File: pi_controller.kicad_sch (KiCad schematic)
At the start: 159 parts, among them J1 PWM, J2 DC Supply, J26 LED6, J27 LED5, J28 LED7, J29 LED8, J30 I2C, J31 UART, J32 LED3, J33 LED1, J34 LED2, J35 LED4, Q1 AOD4184A, Q2 MMBT3904, U1 AP62300TWU, U2 CD74HC4067SM96, U3 LM4040DBZ-3, U4 RaspberryPi_Pico, U5 74HC138, U6 TM1639 (TA2009B), U7 74HC138

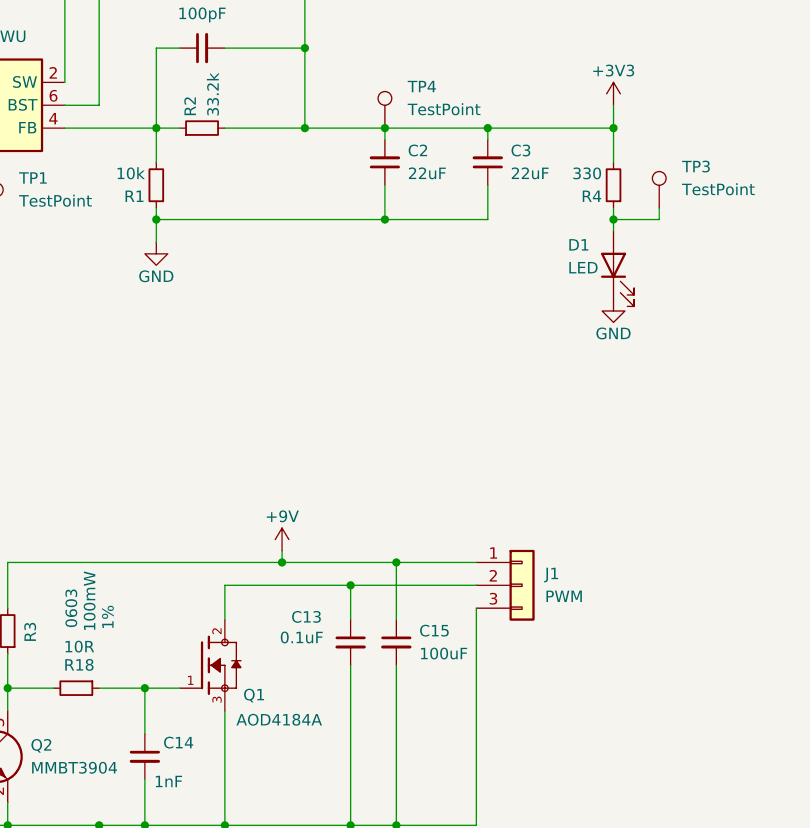
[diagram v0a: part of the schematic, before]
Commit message: Adjusting footprints for production
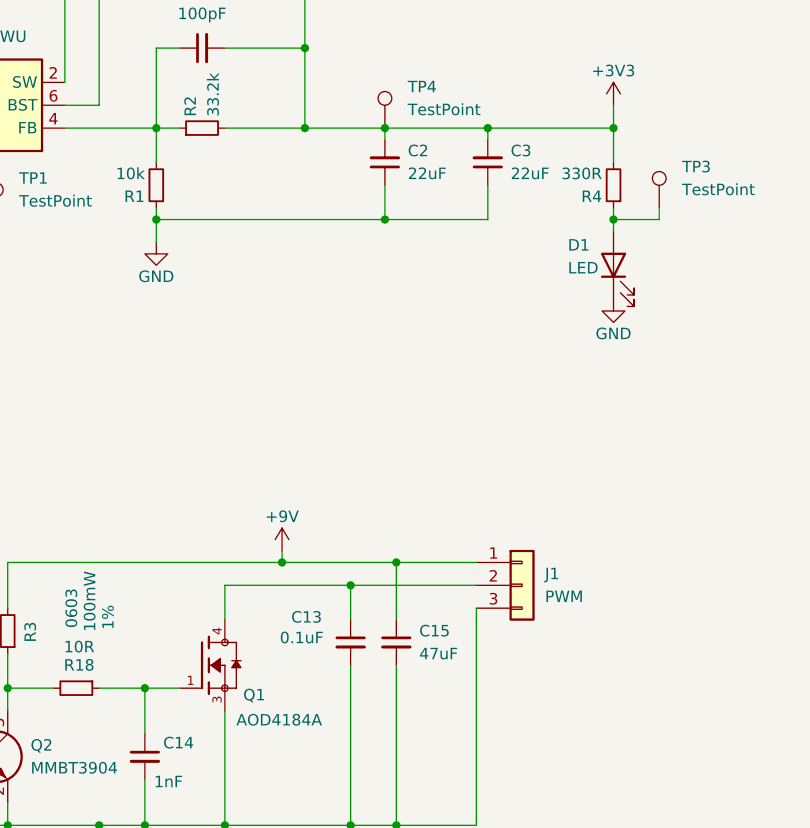
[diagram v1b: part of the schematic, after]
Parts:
- AN1, AN10, AN11, AN12, AN13, AN14, AN15, AN16, AN2, AN3, AN4, AN5, AN6, AN7, AN8, AN9: JLCPCB Part # C495558 -> (none); LCSC PN (none) -> C495558
- C1, C11, C12, C13: footprint Capacitor_SMD:C_0201_0603Metric_Pad0.64x0.40mm_HandSolder -> Capacitor_SMD:C_0603_1608Metric_Pad1.08x0.95mm_HandSolder; JLCPCB Part # C14663 -> (none); LCSC PN (none) -> C14663
- C10: footprint Capacitor_SMD:C_0201_0603Metric_Pad0.64x0.40mm_HandSolder -> Capacitor_SMD:C_1206_3216Metric_Pad1.33x1.80mm_HandSolder; JLCPCB Part # C14663 -> (none); LCSC PN (none) -> C15008; Package 0603 -> 1206
- C14: footprint Capacitor_SMD:C_0201_0603Metric_Pad0.64x0.40mm_HandSolder -> Capacitor_SMD:C_0603_1608Metric_Pad1.08x0.95mm_HandSolder; JLCPCB Part # C1588 -> (none); LCSC PN (none) -> C1588
- C15: value 100uF -> 47uF; footprint Capacitor_SMD:C_0201_0603Metric_Pad0.64x0.40mm_HandSolder -> Capacitor_SMD:C_1206_3216Metric_Pad1.33x1.80mm_HandSolder; JLCPCB Part # C14663 -> (none); LCSC PN (none) -> C76659; Package 0603 -> 1206
- C2, C3: JLCPCB Part # C12891 -> (none); LCSC PN (none) -> C12891
- C4: JLCPCB Part # C13585 -> (none); LCSC PN (none) -> C13585
- C5: JLCPCB Part # C1623 -> (none); LCSC PN (none) -> C1623
- C6: JLCPCB Part # C21120 -> (none); LCSC PN (none) -> C21120
- C7: footprint Capacitor_SMD:C_0201_0603Metric_Pad0.64x0.40mm_HandSolder -> Capacitor_SMD:C_0603_1608Metric_Pad1.08x0.95mm_HandSolder; JLCPCB Part # C14663 -> (none); LCSC PN (none) -> C14858
- C8: footprint Capacitor_SMD:C_0201_0603Metric_Pad0.64x0.40mm_HandSolder -> Capacitor_SMD:C_0603_1608Metric_Pad1.08x0.95mm_HandSolder; JLCPCB Part # C23630 -> (none); LCSC PN (none) -> C23630
- C9: footprint Capacitor_SMD:C_0201_0603Metric_Pad0.64x0.40mm_HandSolder -> Capacitor_SMD:C_0603_1608Metric_Pad1.08x0.95mm_HandSolder; JLCPCB Part # C14663 -> (none); LCSC PN (none) -> C14663; Tolerance 10% -> 5%
- D1: JLCPCB Part # C2297 -> (none); LCSC PN (none) -> C2297
- D10, D11, D12, D13, D14, D15, D16, D17, D18, D19, D2, D20, D21, D22, D23, D24, D25, D26, D27, D28, D29, D3, D30, D31, D32, D33, D34, D35, D36, D37, D38, D39, D4, D40, D41, D42, D43, D44, D45, D46, D47, D48, D49, D5, D50, D51, D52, D53, D54, D55, D56, D57, D58, D59, D6, D60, D61, D62, D63, D64, D65, D7, D8, D9: JLCPCB Part # C358488 -> (none); LCSC PN (none) -> C358488
- J1: JLCPCB Part # C49257 -> (none); LCSC PN (none) -> C49257
- J2: JLCPCB Part # C381116 -> (none); LCSC PN (none) -> C381116
- J26, J27, J28, J29, J32, J33, J34, J35, JR1, JR2, JR3, JR4, JR5, JR6, JR7, JR8: LCSC PN (none) -> C779499
- J30, J31: JLCPCB Part # C163034 -> (none); LCSC PN (none) -> C163034
- JSPI1, JSPI2, JSPI3, JSPI4, JSPI5, JSPI6, JSPI7: JLCPCB Part # C495631 -> (none); LCSC PN (none) -> C495631
- L1: JLCPCB Part # C5189747 -> (none); LCSC PN (none) -> C5189747
- Q1: footprint Package_TO_SOT_SMD:TO-252-2 -> AOD4184A:DPAK228P994X240-4N; JLCPCB Part # C99124 -> (none); LCSC PN (none) -> C99124
- Q2: LCSC PN (none) -> C20526
- R1, R5: JLCPCB Part # C25804 -> (none); LCSC PN (none) -> C25804
- R10, R11, R12, R13, R14, R15, R16, R9: JLCPCB Part # C22978 -> (none); LCSC PN (none) -> C22978
- R17, R7, R8: JLCPCB Part # C4190 -> (none); LCSC PN (none) -> C4190
- R18: JLCPCB Part # C873673 -> (none); LCSC PN (none) -> C22859
- R2: JLCPCB Part # C23003 -> (none); LCSC PN (none) -> C23003
- R3: JLCPCB Part # C543357 -> (none); LCSC PN (none) -> C543357
- R4: value 330 -> 330R; JLCPCB Part # C23137 -> (none); LCSC PN (none) -> C23138
- R6: JLCPCB Part # C23182 -> (none); LCSC PN (none) -> C23182
- U1: JLCPCB Part # C1883519 -> (none); LCSC PN (none) -> C1883519
- U2: JLCPCB Part # C98457 -> (none); LCSC PN (none) -> C98457
- U3: JLCPCB Part # C460608 -> (none); LCSC PN (none) -> C460608
- U4: footprint Module_RaspberryPi_Pico:RaspberryPi_Pico_Common_THT -> PiMatrix:RaspberryPi_Pico_Common_THT_CustomSilk; now left out of the parts list
- U5, U7: JLCPCB Part # C6818 -> (none); LCSC PN (none) -> C6818
- U6: JLCPCB Part # C20611984 -> (none); LCSC PN (none) -> C20611984
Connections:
- net at C13.1, J1.2 (Pin_2): now also Q1.4; no longer Q1.2

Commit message: Project name change to signalbridge and board final revision
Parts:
- AN1, AN10, AN11, AN12, AN13, AN14, AN15, AN16, AN2, AN3, AN4, AN5, AN6, AN7, AN8, AN9: footprint PiMatrix:JST_ZH_B3B-ZR_1x03_P1.50mm_Vertical_SilkSafe -> pi_controller:JST_ZH_B3B-ZR_1x03_P1.50mm_Vertical_SilkSafe
- J2: footprint Connector_BarrelJack:BarrelJack_Horizontal -> pi_controller:BarrelJack_Horizontal
- J26, J27, J28, J29, J32, J33, J34, J35, JR1, JR2, JR3, JR4, JR5, JR6, JR7, JR8: footprint Connector_PinHeader_2.54mm:PinHeader_2x08_P2.54mm_Vertical -> pi_controller:PinHeader_2x08_P2.54mm_Vertical
- J30, J31: footprint PiMatrix:JST_ZH_B4B-ZR_1x04_P1.50mm_Vertical_SilkSafe -> pi_controller:JST_ZH_B4B-ZR_1x04_P1.50mm_Vertical_SilkSafe
- JSPI1, JSPI2, JSPI3, JSPI4, JSPI5, JSPI6, JSPI7: footprint PiMatrix:JST_ZH_B6B-ZR_1x06_P1.50mm_Vertical_SilkSafe -> pi_controller:JST_ZH_B6B-ZR_1x06_P1.50mm_Vertical_SilkSafe
- U4: footprint PiMatrix:RaspberryPi_Pico_Common_THT_CustomSilk -> pi_controller:RaspberryPi_Pico_Common_THT_CustomSilk

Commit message: Changed part number (out of stock)
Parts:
- J26, J27, J28, J29, J32, J33, J34, J35, JR1, JR2, JR3, JR4, JR5, JR6, JR7, JR8: LCSC PN C779499 -> C68234
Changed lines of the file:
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@@
 			)
 		)
-		(property "LCSC PN" "C779499"
+		(property "LCSC PN" "C68234"
 			(at 472.44 236.22 0)
 			(effects
@@
 			)
 		)
-		(property "LCSC PN" "C779499"
+		(property "LCSC PN" "C68234"
 			(at 367.03 149.86 0)
 			(effects
@@
 			)
 		)
-		(property "LCSC PN" "C779499"
+		(property "LCSC PN" "C68234"
 			(at 400.05 121.92 0)
 			(effects
@@
 			)
 		)
-		(property "LCSC PN" "C779499"
+		(property "LCSC PN" "C68234"
 			(at 383.54 276.86 0)
 			(effects
@@
 			)
 		)
-		(property "LCSC PN" "C779499"
+		(property "LCSC PN" "C68234"
 			(at 400.05 180.34 0)
 			(effects
@@
 			)
 		)
-		(property "LCSC PN" "C779499"
+		(property "LCSC PN" "C68234"
 			(at 295.91 320.04 0)
 			(effects
@@
 			)
 		)
-		(property "LCSC PN" "C779499"
+		(property "LCSC PN" "C68234"
 			(at 472.44 278.13 0)
 			(effects
@@
 			)
 		)
-		(property "LCSC PN" "C779499"
+		(property "LCSC PN" "C68234"
 			(at 367.03 179.07 0)
 			(effects
@@
 			)
 		)
-		(property "LCSC PN" "C779499"
+		(property "LCSC PN" "C68234"
 			(at 295.91 276.86 0)
 			(effects
@@
 			)
 		)
-		(property "LCSC PN" "C779499"
+		(property "LCSC PN" "C68234"
 			(at 295.91 234.95 0)
 			(effects
@@
 			)
 		)
-		(property "LCSC PN" "C779499"
+		(property "LCSC PN" "C68234"
 			(at 367.03 91.44 0)
 			(effects
@@
 			)
 		)
-		(property "LCSC PN" "C779499"
+		(property "LCSC PN" "C68234"
 			(at 367.03 120.65 0)
 			(effects
@@
 			)
 		)
-		(property "LCSC PN" "C779499"
+		(property "LCSC PN" "C68234"
 			(at 383.54 320.04 0)
 			(effects
@@
 			)
 		)
-		(property "LCSC PN" "C779499"
+		(property "LCSC PN" "C68234"
 			(at 400.05 151.13 0)
 			(effects
@@
 			)
 		)
-		(property "LCSC PN" "C779499"
+		(property "LCSC PN" "C68234"
 			(at 400.05 92.71 0)
 			(effects
@@
 			)
 		)
-		(property "LCSC PN" "C779499"
+		(property "LCSC PN" "C68234"
 			(at 383.54 234.95 0)
 			(effects

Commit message: Created the slot for the pi and udpated silk screen
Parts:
- added J3, J4: Conn_01x20, Connector_PinHeader_2.54mm:PinHeader_1x20_P2.54mm_Vertical, symbol Connector_Generic:Conn_01x20
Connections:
- net ADC0: now also J4.11 (Pin_11)
- net ADC_MUX_A: now also J4.6 (Pin_6)
- net ADC_MUX_B: now also J4.7 (Pin_7)
- net ADC_MUX_C: now also J4.9 (Pin_9)
- net ADC_MUX_D: now also J3.15 (Pin_15)
- net COL_MUX_A: now also J3.11 (Pin_11)
- net COL_MUX_B: now also J3.12 (Pin_12)
- net COL_MUX_C: now also J3.14 (Pin_14)
- net CS_KEY: now also J4.2 (Pin_2)
- net CS_LED: now also J4.12 (Pin_12)
- net GND: now also J3.13 (Pin_13), J4.13 (Pin_13)
- net MISO: now also J4.1 (Pin_1)
- net MOSI: now also J4.5 (Pin_5)
- net PWM_OUT: now also J4.14 (Pin_14)
- net ROW1: now also J3.1 (Pin_1)
- net ROW2: now also J3.2 (Pin_2)
- net ROW3: now also J3.4 (Pin_4)
- net ROW4: now also J3.5 (Pin_5)
- net ROW5: now also J3.9 (Pin_9)
- net ROW6: now also J3.10 (Pin_10)
- net ROW7: now also J3.19 (Pin_19)
- net ROW8: now also J3.20 (Pin_20)
- net SCL: now also J3.7 (Pin_7)
- net SCLK: now also J4.4 (Pin_4)
- net SDA: now also J3.6 (Pin_6)
- net UART0_RX: now also J3.17 (Pin_17)
- net UART0_TX: now also J3.16 (Pin_16)
- net VDDA: now also J4.15 (Pin_15)
- no-connect marks 8 -> 19

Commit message: Adjusting testpoint pads and adding 74hc4051 datasheet
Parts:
- added C16: 0.1uF, Capacitor_SMD:C_0603_1608Metric_Pad1.08x0.95mm_HandSolder, symbol Device:C_Small
- added U8: CD74HC4051M96, Package_SO:SOIC-16_3.9x9.9mm_P1.27mm, symbol 74xx:74HC4051
- J3, J4: LCSC PN (none) -> C5224030
- TP1, TP2, TP3, TP4: footprint TestPoint:TestPoint_Pad_D4.0mm -> pi_controller:TestPoint_Pad_D2.0mm
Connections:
- net +3V3: now also C16.1, U8.16 (VCC)
- net COL_MUX_A: now also J3.1 (Pin_1), U4.1 (GPIO0); no longer J3.11 (Pin_11), U4.11 (GPIO8), U5.1 (A0)
- net COL_MUX_B: now also J3.2 (Pin_2), U4.2 (GPIO1); no longer J3.12 (Pin_12), U4.12 (GPIO9), U5.2 (A1)
- net COL_MUX_C: now also J3.4 (Pin_4), U4.4 (GPIO2); no longer J3.14 (Pin_14), U4.14 (GPIO10), U5.3 (A2)
- net GND: now also C16.2, U8.7 (VEE), U8.8 (GND)
- net ROW1: now also U8.13 (A0); no longer J3.1 (Pin_1), U4.1 (GPIO0)
- net ROW2: now also U8.14 (A1); no longer J3.2 (Pin_2), U4.2 (GPIO1)
- net ROW3: now also U8.15 (A2); no longer J3.4 (Pin_4), U4.4 (GPIO2)
- net ROW4: now also U8.12 (A3); no longer J3.5 (Pin_5), U4.5 (GPIO3)
- net ROW5: now also U8.1 (A4); no longer J3.9 (Pin_9), U4.9 (GPIO6)
- net ROW6: now also U8.5 (A5); no longer J3.10 (Pin_10), U4.10 (GPIO7)
- net ROW7: now also U8.2 (A6); no longer J3.19 (Pin_19), U4.19 (GPIO14)
- net ROW8: now also U8.4 (A7); no longer J3.20 (Pin_20), U4.20 (GPIO15)
- net CS_KEY renamed CS_COL
- net CS_LED renamed SPI_MUX_CS
- new net CS_ROW: J3.11 (Pin_11), U4.11 (GPIO8), U8.6 (~{E})
- new net ROW_INPUT: J3.12 (Pin_12), U4.12 (GPIO9), U8.3 (A)
- new net ROW_MUX_A: J3.9 (Pin_9), U4.9 (GPIO6), U8.11 (S0)
- new net ROW_MUX_B: J3.10 (Pin_10), U4.10 (GPIO7), U8.10 (S1)
- new net ROW_MUX_C: J3.5 (Pin_5), U4.5 (GPIO3), U8.9 (S2)
- new net SPI_MUX_A: J3.14 (Pin_14), U4.14 (GPIO10), U5.1 (A0)
- new net SPI_MUX_B: J3.19 (Pin_19), U4.19 (GPIO14), U5.2 (A1)
- new net SPI_MUX_C: J3.20 (Pin_20), U4.20 (GPIO15), U5.3 (A2)
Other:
- moved on the sheet: C12, U7

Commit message: Upgrading power supply protection
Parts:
- added C17: 22uF, Capacitor_SMD:C_1206_3216Metric_Pad1.33x1.80mm_HandSolder, symbol Device:C_Small
- added D66: Z2SMBJ18A, Diode_SMD:D_SMB, symbol Diode:Z2SMBxxx
- added D67: BZT52C12, Diode_SMD:D_SOD-123, symbol Diode:BZT52Bxx
- added F1: Polyfuse, Fuse:Fuse_1210_3225Metric_Pad1.42x2.65mm_HandSolder, symbol Device:Polyfuse
- added JP1: Jumper_2_Open, Jumper:SolderJumper-2_P1.3mm_Open_TrianglePad1.0x1.5mm, symbol Jumper:Jumper_2_Open
- added Q3: AO4407A, AO4407A:SOIC127P600X175-8N, symbol AO4407A:AO4407A
- added R19, R20, R21, R22, R23, R24, R25, R26, R27, R28, R29: 4.7k, Resistor_SMD:R_0603_1608Metric_Pad0.98x0.95mm_HandSolder, symbol Device:R_Small
- added R30: 10k, Resistor_SMD:R_0603_1608Metric_Pad0.98x0.95mm_HandSolder, symbol Device:R_Small
- added TP5, TP6: TestPoint, pi_controller:TestPoint_Pad_D2.0mm, symbol Connector:TestPoint
- C15: Voltage Rating 50V -> 25V
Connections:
- net +3V3: now also R19.1, R20.1, R21.1, R22.1, R23.1, R24.1, R25.1, R26.1, R27.1, R28.1, R29.1
- net +9V: now also F1.1; no longer C4.2, U1.3 (IN)
- net CS1: now also R19.2
- net CS2: now also R20.2
- net CS3: now also R21.2
- net CS4: now also R22.2
- net CS5: now also R23.2
- net CS6: now also R24.2
- net CS7: now also R25.2
- net CS8: now also R26.2
- net GND: now also C17.1, D66.2 (A), R30.1
- net MISO: now also R28.2
- net MOSI: now also R27.2
- net PWM_OUT: now also TP5.1
- net SCLK: now also R29.2
- new net: C17.2, C4.2, D67.1 (K), JP1.2 (B), Q3.1, Q3.2, Q3.3, TP6.1, U1.3 (IN)
- new net: D66.1 (K), F1.2, JP1.1 (A), Q3.5, Q3.6, Q3.7, Q3.8
- new net: D67.2 (A), Q3.4, R30.2
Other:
- note added: "PWM Output Power Suuply / max 5A"
- note removed: "PWM Output 9V / max 5A"
- title: PiMax - Raspberry Pi Pico Breakout Board -> SignalBridge - Raspberry Pi Pico Breakout Board
- moved on the sheet: C2, C3, C4, C5, C6, C7, C9, D1, J2, L1, R1, R2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

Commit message: Adding power supply protection, ground pour in the top and new 3d models
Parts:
- J1: footprint Connector_PinHeader_2.54mm:PinHeader_1x03_P2.54mm_Vertical -> pi_controller:JST_ZH_B3B-ZR_1x03_P1.50mm_Vertical_SilkSafe; LCSC PN C49257 -> C495558
- J3, J4: footprint Connector_PinHeader_2.54mm:PinHeader_1x20_P2.54mm_Vertical -> Connector_PinSocket_2.54mm:PinSocket_1x20_P2.54mm_Vertical
- JP1: footprint Jumper:SolderJumper-2_P1.3mm_Open_TrianglePad1.0x1.5mm -> pi_controller:SolderJumper-2_P1.3mm_Open_TrianglePad1.0x1.5mm_Silk
- U6: footprint Package_SO:SOP-24_7.5x15.4mm_P1.27mm -> pi_controller:SOP-24_7.5x15.4mm_P1.27mm
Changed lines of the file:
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@@
 			)
 		)
-		(property "Footprint" "Jumper:SolderJumper-2_P1.3mm_Open_TrianglePad1.0x1.5mm"
+		(property "Footprint" "pi_controller:SolderJumper-2_P1.3mm_Open_TrianglePad1.0x1.5mm_Silk"
 			(at 59.69 57.15 0)
 			(effects
@@
 			)
 		)
-		(property "Footprint" "Connector_PinHeader_2.54mm:PinHeader_1x20_P2.54mm_Vertical"
+		(property "Footprint" "Connector_PinSocket_2.54mm:PinSocket_1x20_P2.54mm_Vertical"
 			(at 120.65 368.3 0)
 			(effects
@@
 			)
 		)
-		(property "Footprint" "Connector_PinHeader_2.54mm:PinHeader_1x20_P2.54mm_Vertical"
+		(property "Footprint" "Connector_PinSocket_2.54mm:PinSocket_1x20_P2.54mm_Vertical"
 			(at 82.55 368.3 0)
 			(effects
@@
 			)
 		)
-		(property "Footprint" "Package_SO:SOP-24_7.5x15.4mm_P1.27mm"
+		(property "Footprint" "pi_controller:SOP-24_7.5x15.4mm_P1.27mm"
 			(at 346.71 135.89 0)
 			(effects
@@
 			)
 		)
-		(property "Footprint" "Connector_PinHeader_2.54mm:PinHeader_1x03_P2.54mm_Vertical"
+		(property "Footprint" "pi_controller:JST_ZH_B3B-ZR_1x03_P1.50mm_Vertical_SilkSafe"
 			(at 148.59 125.73 0)
 			(effects
@@
 			)
 		)
-		(property "Description" "Generic connector, single row, 01x03, script generated (kicad-library-utils/schlib/autogen/connector/)"
+		(property "Description" "JST-ZH"
 			(at 148.59 125.73 0)
 			(effects
@@
 			)
 		)
-		(property "LCSC PN" "C49257"
+		(property "LCSC PN" "C495558"
 			(at 148.59 125.73 0)
 			(effects

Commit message: Adjusting DRC setting
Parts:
- D1: symbol Device:LED -> Signalbridge:LED
- Q1: symbol AOD4184A:AOD4184A -> Signalbridge:AOD4184A
- Q2: symbol Transistor_BJT:MMBT3904 -> Signalbridge:MMBT3904
- R1, R10, R11, R12, R13, R14, R15, R16, R17, R18, R19, R2, R20, R21, R22, R23, R24, R25, R26, R27, R28, R29, R3, R30, R4, R5, R6, R7, R8, R9: symbol Device:R_Small -> Signalbridge:R_Small
- U1: symbol Regulator_Switching:AP62300TWU -> Signalbridge:AP62300TWU
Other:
- moved on the sheet: AN1, AN10, AN11, AN12, AN13, AN14, AN15, AN16, AN2, AN3, AN4, AN5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
